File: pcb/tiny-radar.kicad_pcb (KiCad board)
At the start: 2 copper layers, 100 x 50 mm, 112 parts, among them P201 USB_OTG, P202 CONN_01X04, P203 CONN_01X04, P401 CONN_01X02, P402 CONN_01X02, U201 AP2114H, U202 STM32F072CBU, U301 INA826AIDRG, U302 LMV321LILT, U303 LMV321LILT, U304 LMV321LILT, U401 MAX2750, U402 MGA-635P8, U403 HHM1520, U404 MGA-635P8, U405 LT5560, U406 PD2328J, U407 WA04P

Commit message: board ready to route
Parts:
- moved C205 0.50 mm to (142.5, 75.8)
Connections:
- C414 pad 1: (no net) -> /RF/MIXER_IN
- U403 pad 1: (no net) -> /RF/MIXER_IN
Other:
- board size 100 x 50 mm -> 94.5 x 28.5 mm
- net class Default: clearance 0.2 -> 0.13; trace_width 0.25 -> 0.13; via_dia 0.6 -> 0.46; via_drill 0.4 -> 0.26
- rule trace_clearance: 0.2 -> 0.13
- rule trace_min: 0.2 -> 0.13
- rule via_min_drill: 0.3 -> 0.26
- rule via_min_size: 0.4 -> 0.46
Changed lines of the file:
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@@
 (kicad_pcb (version 4) (host pcbnew 4.0.5-e0-6337~49~ubuntu14.04.1)
   (general
-    (links 243)
-    (no_connects 243)
+    (links 244)
+    (no_connects 244)
     (area 111.924999 57.924999 212.075001 108.075001)
     (thickness 1.6)
@@
     (zones 0)
     (modules 112)
-    (nets 69)
+    (nets 70)
   )
   (page A4)
@@
   )
   (setup
-    (last_trace_width 0.25)
-    (trace_clearance 0.2)
+    (last_trace_width 0.38)
+    (user_trace_width 0.13)
+    (user_trace_width 0.24)
+    (user_trace_width 0.36)
+    (user_trace_width 0.38)
+    (user_trace_width 0.48)
+    (user_trace_width 0.64)
+    (trace_clearance 0.13)
     (zone_clearance 0.508)
     (zone_45_only no)
-    (trace_min 0.2)
+    (trace_min 0.13)
     (segment_width 0.2)
     (edge_width 0.15)
-    (via_size 0.6)
-    (via_drill 0.4)
-    (via_min_size 0.4)
-    (via_min_drill 0.3)
+    (via_size 0.46)
+    (via_drill 0.26)
+    (via_min_size 0.46)
+    (via_min_drill 0.26)
+    (user_via 0.46 0.26)
+    (user_via 0.6 0.38)
+    (user_via 0.8 0.64)
+    (user_via 1 0.74)
     (uvia_size 0.3)
     (uvia_drill 0.1)
@@
   (net 67 "Net-(R410-Pad2)")
   (net 68 "Net-(C406-Pad2)")
+  (net 69 /RF/MIXER_IN)
   (net_class Default "This is the default net class."
-    (clearance 0.2)
-    (trace_width 0.25)
-    (via_dia 0.6)
-    (via_drill 0.4)
+    (clearance 0.13)
+    (trace_width 0.13)
+    (via_dia 0.46)
+    (via_drill 0.26)
     (uvia_dia 0.3)
     (uvia_drill 0.1)
@@
     (add_net /Control/USB_P)
     (add_net /Control/VDDA)
+    (add_net /RF/MIXER_IN)
     (add_net /RF/MIXER_IN+)
     (add_net /RF/MIXER_IN-)
@@
   )
   (module Capacitors_SMD:C_0603 (layer F.Cu)
-    (at 142 75.75 90)
+    (at 142.5 75.75 90)
     (descr "Capacitor SMD 0603, reflow soldering, AVX (see smccp.pdf)")
     (tags "capacitor 0603")
@@
     (fp_line (start 0.25 -0.475) (end -0.25 -0.475) (layer F.SilkS) (width 0.12))
     (fp_line (start -0.25 0.475) (end 0.25 0.475) (layer F.SilkS) (width 0.12))
-    (pad 1 smd rect (at -0.55 0) (size 0.6 0.5) (layers F.Cu F.Paste F.Mask))
+    (pad 1 smd rect (at -0.55 0) (size 0.6 0.5) (layers F.Cu F.Paste F.Mask)
+      (net 69 /RF/MIXER_IN))
     (pad 2 smd rect (at 0.55 0) (size 0.6 0.5) (layers F.Cu F.Paste F.Mask)
       (net 29 "Net-(C414-Pad2)"))
@@
     )
     (fp_line (start -1.25 -0.75) (end -1.25 0.75) (layer F.SilkS) (width 0.3))
-    (pad 1 smd rect (at -0.65 0.65 180) (size 0.3 0.8) (layers F.Cu F.Paste F.Mask))
+    (pad 1 smd rect (at -0.65 0.65 180) (size 0.3 0.8) (layers F.Cu F.Paste F.Mask)
+      (net 69 /RF/MIXER_IN))
     (pad 2 smd rect (at 0 0.65 180) (size 0.3 0.8) (layers F.Cu F.Paste F.Mask)
       (net 60 "Net-(R404-Pad2)"))
@@
     )
   )
-  (gr_line (start 112 108) (end 112 58) (angle 90) (layer Edge.Cuts) (width 0.15))
-  (gr_line (start 212 108) (end 112 108) (angle 90) (layer Edge.Cuts) (width 0.15))
-  (gr_line (start 212 58) (end 212 108) (angle 90) (layer Edge.Cuts) (width 0.15))
-  (gr_line (start 112 58) (end 212 58) (angle 90) (layer Edge.Cuts) (width 0.15))
+  (gr_line (start 212 91.5) (end 212 64) (layer Edge.Cuts) (width 0.15))
+  (gr_line (start 117.5 91.5) (end 212 91.5) (layer Edge.Cuts) (width 0.15))
+  (gr_line (start 117.5 64) (end 117.5 92.5) (layer Edge.Cuts) (width 0.15))
+  (gr_line (start 212 64) (end 117.5 64) (layer Edge.Cuts) (width 0.15))
 )

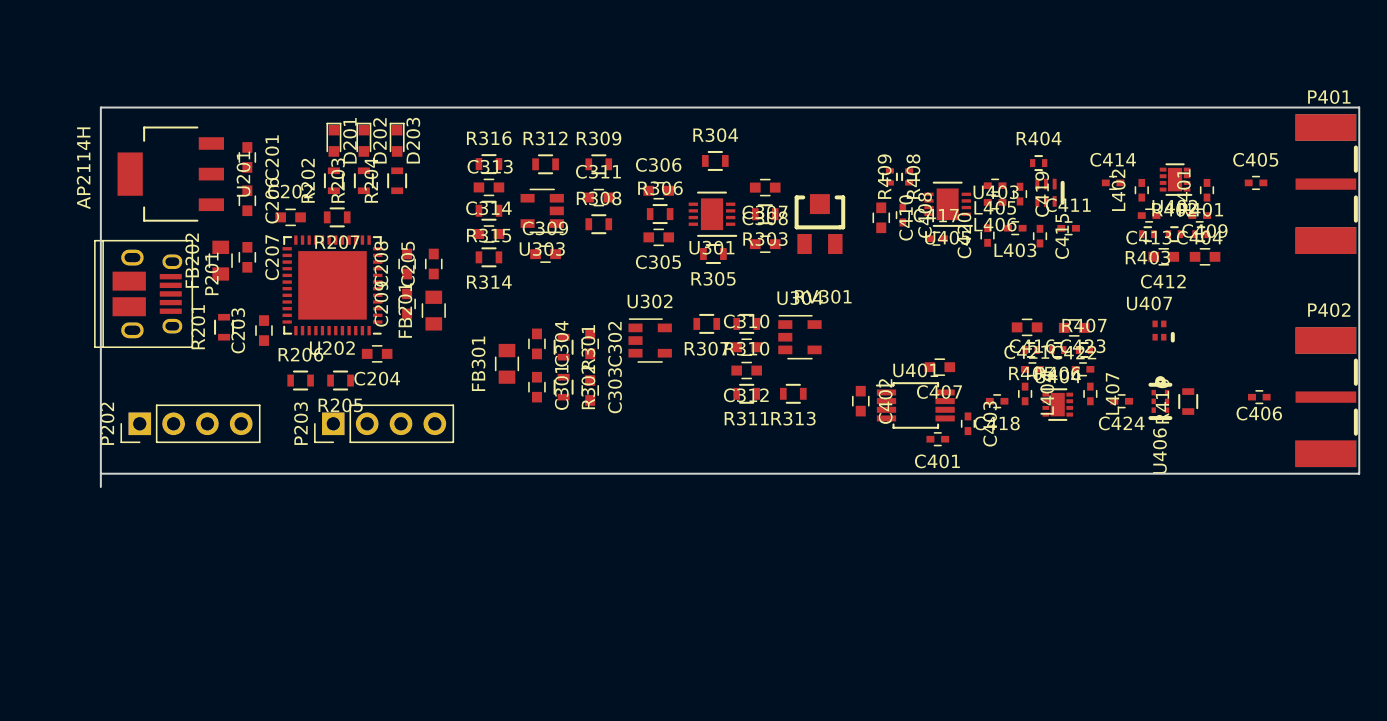
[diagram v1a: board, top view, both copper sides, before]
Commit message: finished PCB routing, begin design review
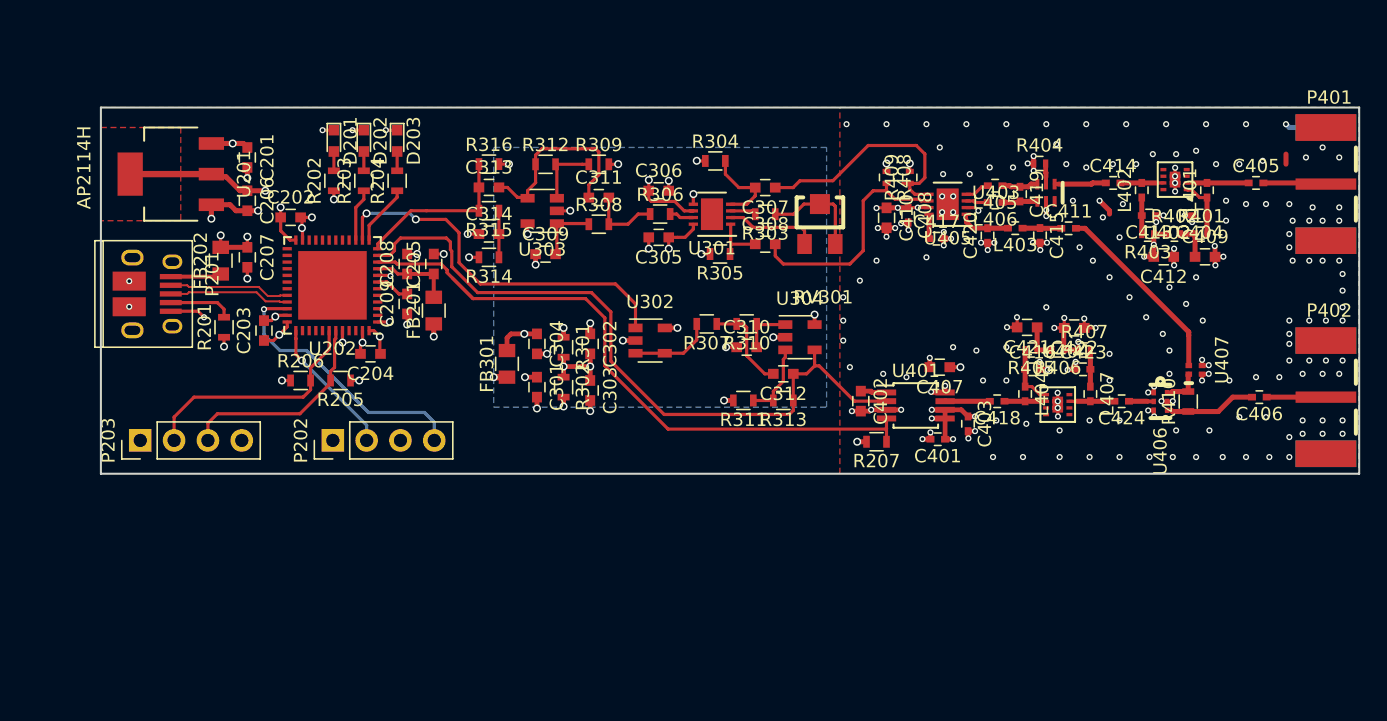
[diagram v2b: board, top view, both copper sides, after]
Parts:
- U402, U404: footprint Housings_DFN_QFN:DFN-8-1EP_2x2mm_Pitch0.5mm -> wbraun_smd:8-QFN-2x2
- moved R207 43.9 mm to (175.8, 89.1)
- moved P203 14.6 mm to (120.5, 89.0)
- moved P202 14.6 mm to (134.9, 89.0)
- moved U407 4.00 mm to (199.7, 83.7), turned to 90 degrees
- moved C312 2.76 mm to (168.8, 84.0)
- moved R313 0.90 mm to (168.8, 86.0)
- moved R311 0.56 mm to (165.8, 86.0)
- moved C204 0.50 mm to (137.8, 82.5)
- moved R305 0.50 mm to (164.0, 75.0)
- moved C408 0.40 mm to (178.1, 72.1)
- moved C410 0.40 mm to (176.5, 72.3)
- moved R408 0.26 mm to (176.5, 69.2)
- moved R404 0.08 mm to (188.0, 68.2)
- moved R409 0.07 mm to (178.2, 69.2)
- moved C415 0.06 mm to (188.0, 73.6)
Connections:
- net /Control/VDDA renamed /Control/VDDA2
- C307 pad 1: /Analog/IF+ -> /Analog/IF-
- C308 pad 2: /Analog/IF- -> /Analog/IF+
- C309 pad 1: /Analog/VDD/2 -> /Analog/VDDA/2
- R303 pad 2: /Analog/RG2 -> /Analog/RG1
- R309 pad 2: /Analog/VDD/2 -> /Analog/VDDA/2
- RV301 pad 1: /Analog/RG1 -> Net-(R303-Pad1)
- RV301 pad 3: Net-(R303-Pad1) -> /Analog/RG2
- U202 pad 10: (no net) -> /Control/RF_ENABLE
- U202 pad 16: /Control/RF_ENABLE -> (no net)
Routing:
- net GND: track 0.00 -> 374.1 mm, vias 0 -> 230
- net +5V: track 0.00 -> 105.7 mm, vias 0 -> 15
- net /Analog/ADC_RAMP: track 0.00 -> 53.1 mm
- net /Control/RF_ENABLE: track 0.00 -> 49.6 mm
- net +3V3: track 0.00 -> 31.3 mm, vias 0 -> 15
- net /Analog/RAMP_DAC: track 0.00 -> 28.3 mm, vias 0 -> 2
- net /Control/SWDIO: track 0.00 -> 20.5 mm, vias 0 -> 1
- net /Analog/IF-: track 0.00 -> 18.6 mm
- net /Analog/IF+: track 0.00 -> 18.0 mm
- net /Control/SCL: track 0.00 -> 17.9 mm
- net /Control/SDA: track 0.00 -> 15.9 mm
- net /Analog/VDDA/2: track 0.00 -> 15.3 mm, vias 0 -> 9
- net Net-(C311-Pad1): track 0.00 -> 14.8 mm
- net /RF/MIXER_LO: track 0.00 -> 14.2 mm
- net /Analog/IF_ADC: track 0.00 -> 12.5 mm
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- added copper zone on F.Cu, net +3V3
- added copper zone on In2.Cu, net +3V3
- added copper zone on In2.Cu, net +5V
- added copper zone on In2.Cu, net /Analog/VDDA
- added copper zone on B.Cu, net /Analog/VDDA/2
- added copper zone on B.Cu, net GND
- added copper zone on F.Cu, net GND
- added copper zone on In1.Cu, net GND
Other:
- board size 94.5 x 28.5 mm -> 94.5 x 27.5 mm
- copper layers 2 -> 4
- rule pad_to_mask_clearance: 0.2 -> 0.064
